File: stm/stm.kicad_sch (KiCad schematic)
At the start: 0 parts

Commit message: added power sch
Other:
- added sheet power (power.kicad_sch)
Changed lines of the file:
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@@
+	)
+	(sheet
+		(at 57.15 93.98)
+		(size 53.34 30.48)
+		(exclude_from_sim no)
+		(in_bom yes)
+		(on_board yes)
+		(dnp no)
+		(fields_autoplaced yes)
+		(stroke
+			(width 0.1524)
+			(type solid)
+		)
+		(fill
+			(color 0 0 0 0.0000)
+		)
+		(property "Sheetname" "power"
+			(at 57.15 93.2684 0)
+			(effects
+				(font
+					(size 1.27 1.27)
+				)
+				(justify left bottom)
+			)
+		)
+		(property "Sheetfile" "power.kicad_sch"
+			(at 57.15 125.0446 0)
+			(effects
+				(font
+					(size 1.27 1.27)
+				)
+				(justify left top)
+			)
+		)
+		(instances
+			(project "stm"
+				(path "/8c38e4ab-00b4-41d2-ba83-c24ee9e4f60d"
+					(page "4")
+				)
+			)
+		)
 	)
 	(sheet

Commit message: usbc power and uart
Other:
- added sheet peripherals (peripherals.kicad_sch)
- added sheet usb to uart (usb_to_uart.kicad_sch)
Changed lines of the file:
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@@
 	(paper "A")
+	(sheet
+		(at 123.19 93.98)
+		(size 52.07 30.48)
+		(exclude_from_sim no)
+		(in_bom yes)
+		(on_board yes)
+		(dnp no)
+		(fields_autoplaced yes)
+		(stroke
+			(width 0.1524)
+			(type solid)
+		)
+		(fill
+			(color 0 0 0 0.0000)
+		)
+		(property "Sheetname" "peripherals"
+			(at 123.19 93.2684 0)
+			(effects
+				(font
+					(size 1.27 1.27)
+				)
+				(justify left bottom)
+			)
+		)
+		(property "Sheetfile" "peripherals.kicad_sch"
+			(at 123.19 125.0446 0)
+			(effects
+				(font
+					(size 1.27 1.27)
+				)
+				(justify left top)
+			)
+		)
+		(instances
+			(project "stm"
+				(path "/8c38e4ab-00b4-41d2-ba83-c24ee9e4f60d"
+					(page "5")
+				)
+			)
+		)
+	)
 	(sheet
 		(at 57.15 49.53)
@@
 				)
 			)
+		)
+	)
+	(sheet
+		(at 181.61 93.98)
+		(size 44.45 30.48)
+		(exclude_from_sim no)
+		(in_bom yes)
+		(on_board yes)
+		(dnp no)
+		(fields_autoplaced yes)
+		(stroke
+			(width 0.1524)
+			(type solid)
+		)
+		(fill
+			(color 0 0 0 0.0000)
+		)
+		(property "Sheetname" "usb to uart"
+			(at 181.61 93.2684 0)
+			(effects
+				(font
+					(size 1.27 1.27)
+				)
+				(justify left bottom)
+			)
+		)
+		(property "Sheetfile" "usb_to_uart.kicad_sch"
+			(at 181.61 125.0446 0)
+			(effects
+				(font
+					(size 1.27 1.27)
+				)
+				(justify left top)
+			)
+		)
+		(instances
+			(project "stm"
+				(path "/8c38e4ab-00b4-41d2-ba83-c24ee9e4f60d"
+					(page "6")
+				)
+			)

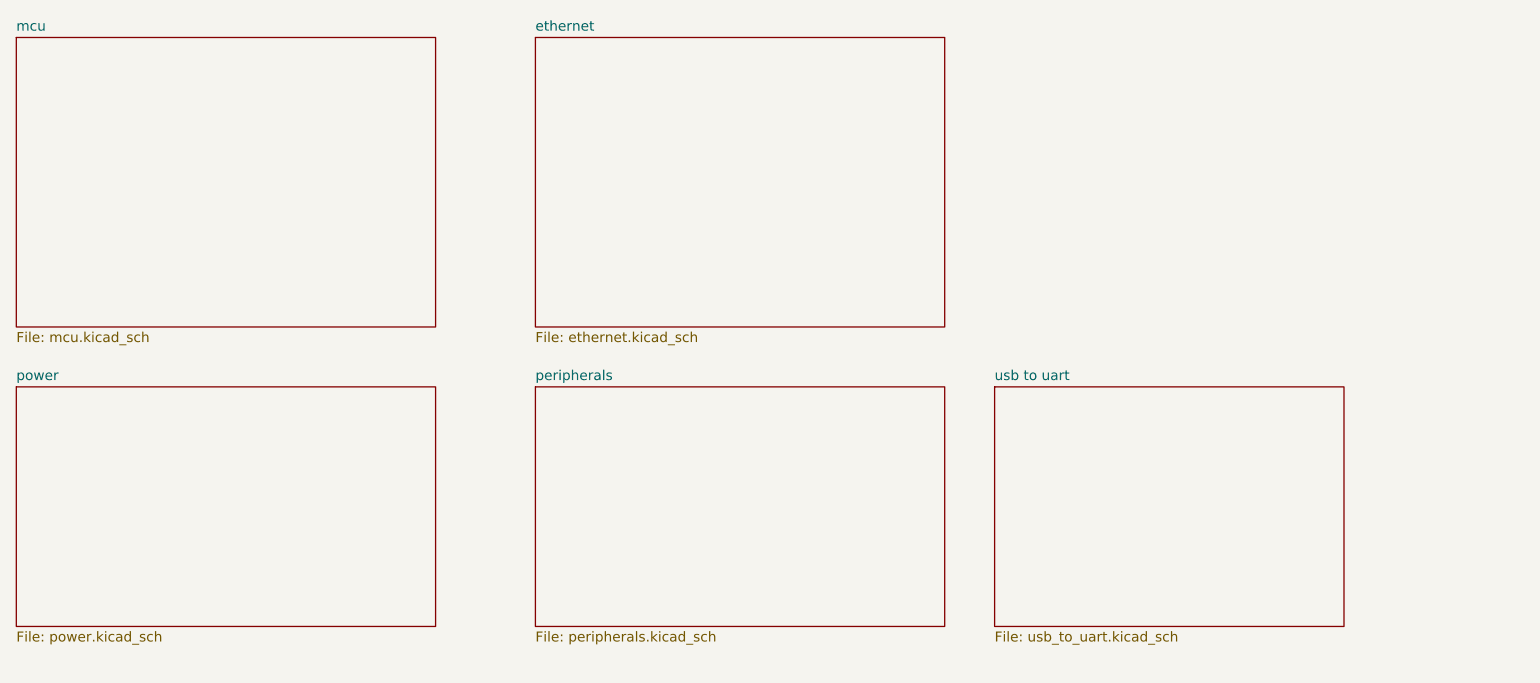
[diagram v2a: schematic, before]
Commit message: PE and PF pin connectors
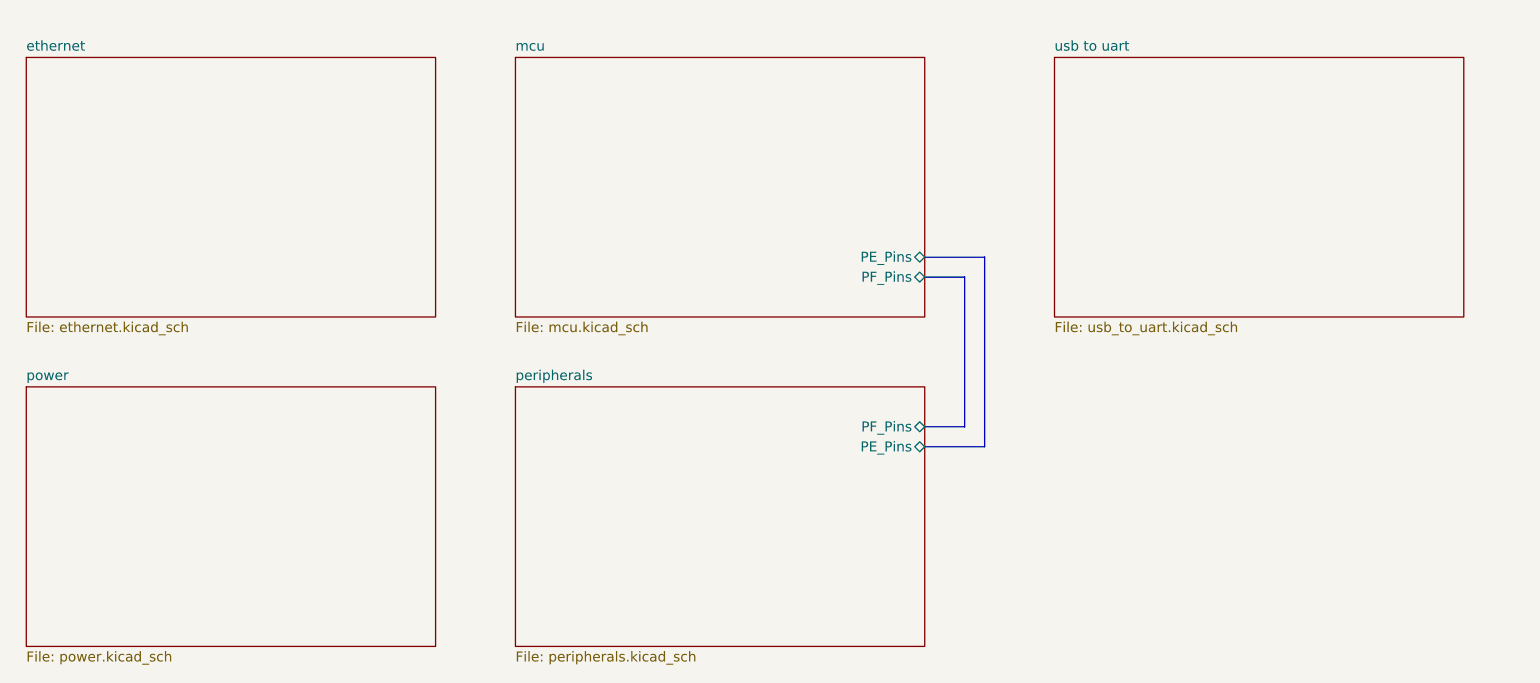
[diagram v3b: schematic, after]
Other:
- sheet mcu ports: added PE_Pins, PF_Pins; removed none
- sheet peripherals ports: added PE_Pins, PF_Pins; removed none
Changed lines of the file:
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@@
 	(generator_version "9.0")
 	(paper "A")
-	(sheet
-		(at 123.19 93.98)
-		(size 52.07 30.48)
+	(bus
+		(pts
+			(xy 177.8 99.06) (xy 177.8 80.01)
+		)
+		(stroke
+			(width 0)
+			(type default)
+		)
+	)
+	(bus
+		(pts
+			(xy 177.8 99.06) (xy 172.72 99.06)
+		)
+		(stroke
+			(width 0)
+			(type default)
+		)
+	)
+	(bus
+		(pts
+			(xy 172.72 77.47) (xy 180.34 77.47)
+		)
+		(stroke
+			(width 0)
+			(type default)
+		)
+	)
+	(bus
+		(pts
+			(xy 172.72 80.01) (xy 177.8 80.01)
+		)
+		(stroke
+			(width 0)
+			(type default)
+		)
+	)
+	(bus
+		(pts
+			(xy 180.34 77.47) (xy 180.34 101.6)
+		)
+		(stroke
+			(width 0)
+			(type default)
+		)
+	)
+	(bus
+		(pts
+			(xy 180.34 101.6) (xy 172.72 101.6)
+		)
+		(stroke
+			(width 0)
+			(type default)
+		)
+	)
+	(sheet
+		(at 120.65 93.98)
+		(size 52.07 33.02)
 		(exclude_from_sim no)
 		(in_bom yes)
@@
 		)
 		(property "Sheetname" "peripherals"
-			(at 123.19 93.2684 0)
+			(at 120.65 93.2684 0)
 			(effects
 				(font
@@
 		)
 		(property "Sheetfile" "peripherals.kicad_sch"
-			(at 123.19 125.0446 0)
-			(effects
-				(font
-					(size 1.27 1.27)
-				)
-				(justify left top)
+			(at 120.65 127.5846 0)
+			(effects
+				(font
+					(size 1.27 1.27)
+				)
+				(justify left top)
+			)
+		)
+		(pin "PE_Pins" bidirectional
+			(at 172.72 101.6 0)
+			(effects
+				(font
+					(size 1.27 1.27)
+				)
+				(justify right)
+			)
+		)
+		(pin "PF_Pins" bidirectional
+			(at 172.72 99.06 0)
+			(effects
+				(font
+					(size 1.27 1.27)
+				)
+				(justify right)
 			)
 		)
@@
 	)
 	(sheet
-		(at 57.15 49.53)
-		(size 53.34 36.83)
+		(at 120.65 52.07)
+		(size 52.07 33.02)
 		(exclude_from_sim no)
 		(in_bom yes)
@@
 		)
 		(property "Sheetname" "mcu"
-			(at 57.15 48.8184 0)
+			(at 120.65 51.3584 0)
 			(effects
 				(font
@@
 		)
 		(property "Sheetfile" "mcu.kicad_sch"
-			(at 57.15 86.9446 0)
-			(effects
-				(font
-					(size 1.27 1.27)
-				)
-				(justify left top)
+			(at 120.65 85.6746 0)
+			(effects
+				(font
+					(size 1.27 1.27)
+				)
+				(justify left top)
+			)
+		)
+		(pin "PE_Pins" bidirectional
+			(at 172.72 77.47 0)
+			(effects
+				(font
+					(size 1.27 1.27)
+				)
+				(justify right)
+			)
+		)
+		(pin "PF_Pins" bidirectional
+			(at 172.72 80.01 0)
+			(effects
+				(font
+					(size 1.27 1.27)
+				)
+				(justify right)
 			)
 		)
@@
 	)
 	(sheet
-		(at 57.15 93.98)
-		(size 53.34 30.48)
+		(at 58.42 93.98)
+		(size 52.07 33.02)
 		(exclude_from_sim no)
 		(in_bom yes)
@@
 		)
 		(property "Sheetname" "power"
-			(at 57.15 93.2684 0)
+			(at 58.42 93.2684 0)
 			(effects
 				(font
@@
 		)
 		(property "Sheetfile" "power.kicad_sch"
-			(at 57.15 125.0446 0)
+			(at 58.42 127.5846 0)
 			(effects
 				(font
@@
 	)
 	(sheet
-		(at 123.19 49.53)
-		(size 52.07 36.83)
+		(at 58.42 52.07)
+		(size 52.07 33.02)
 		(exclude_from_sim no)
 		(in_bom yes)
@@
 		)
 		(property "Sheetname" "ethernet"
-			(at 123.19 48.8184 0)
+			(at 58.42 51.3584 0)
 			(effects
 				(font
@@
 		)
 		(property "Sheetfile" "ethernet.kicad_sch"
-			(at 123.19 86.9446 0)
+			(at 58.42 85.6746 0)
 			(effects
 				(font
@@
 	)
 	(sheet
-		(at 181.61 93.98)
-		(size 44.45 30.48)
+		(at 189.23 52.07)
+		(size 52.07 33.02)
 		(exclude_from_sim no)
 		(in_bom yes)
@@
 		)
 		(property "Sheetname" "usb to uart"
-			(at 181.61 93.2684 0)
+			(at 189.23 51.3584 0)
 			(effects
 				(font
@@
 		)
 		(property "Sheetfile" "usb_to_uart.kicad_sch"
-			(at 181.61 125.0446 0)
-			(effects
-				(font
+			(at 189.23 85.6746 0)
+			(effects
+				(font

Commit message: completed peripherals mapping
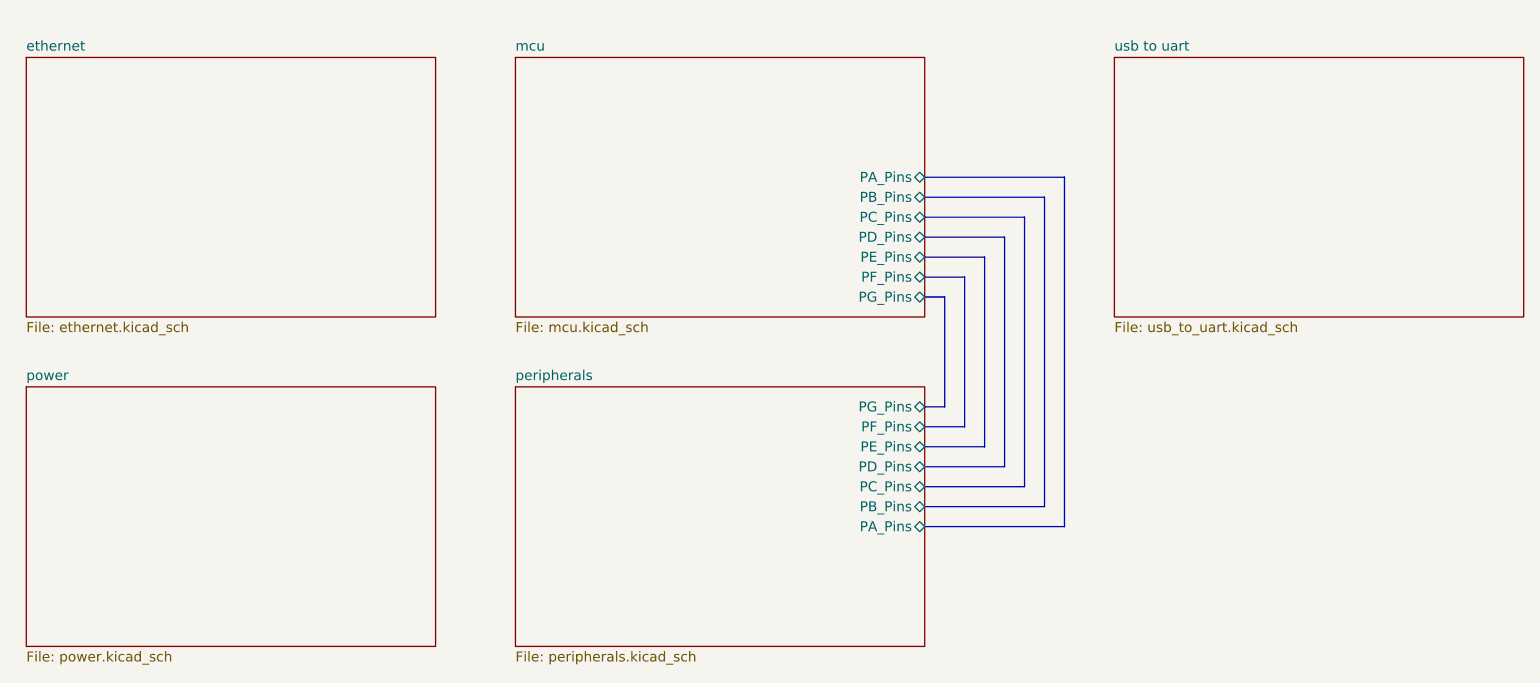
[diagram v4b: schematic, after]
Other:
- sheet mcu ports: added PA_Pins, PB_Pins, PC_Pins, PD_Pins, PG_Pins; removed none
- sheet peripherals ports: added PA_Pins, PB_Pins, PC_Pins, PD_Pins, PG_Pins; removed none
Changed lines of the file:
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@@
+	(bus
+		(pts
+			(xy 187.96 109.22) (xy 187.96 69.85)
+		)
+		(stroke
+			(width 0)
+			(type default)
+		)
+	)
+	(bus
+		(pts
+			(xy 172.72 111.76) (xy 190.5 111.76)
+		)
+		(stroke
+			(width 0)
+			(type default)
+		)
+	)
+	(bus
+		(pts
+			(xy 172.72 104.14) (xy 182.88 104.14)
+		)
+		(stroke
+			(width 0)
+			(type default)
+		)
+	)
+	(bus
+		(pts
+			(xy 172.72 69.85) (xy 187.96 69.85)
+		)
+		(stroke
+			(width 0)
+			(type default)
+		)
+	)
+	(bus
+		(pts
+			(xy 175.26 96.52) (xy 172.72 96.52)
+		)
+		(stroke
+			(width 0)
+			(type default)
+		)
+	)
+	(bus
+		(pts
+			(xy 172.72 67.31) (xy 190.5 67.31)
+		)
+		(stroke
+			(width 0)
+			(type default)
+		)
+	)
+	(bus
+		(pts
+			(xy 172.72 82.55) (xy 175.26 82.55)
+		)
+		(stroke
+			(width 0)
+			(type default)
+		)
+	)
+	(bus
+		(pts
+			(xy 182.88 104.14) (xy 182.88 74.93)
+		)
+		(stroke
+			(width 0)
+			(type default)
+		)
+	)
+	(bus
+		(pts
+			(xy 190.5 67.31) (xy 190.5 111.76)
+		)
+		(stroke
+			(width 0)
+			(type default)
+		)
+	)
+	(bus
+		(pts
+			(xy 185.42 72.39) (xy 185.42 106.68)
+		)
+		(stroke
+			(width 0)
+			(type default)
+		)
+	)
+	(bus
+		(pts
+			(xy 172.72 72.39) (xy 185.42 72.39)
+		)
+		(stroke
+			(width 0)
+			(type default)
+		)
+	)
+	(bus
+		(pts
+			(xy 172.72 109.22) (xy 187.96 109.22)
+		)
+		(stroke
+			(width 0)
+			(type default)
+		)
+	)
 	(bus
 		(pts
@@
 	(bus
 		(pts
+			(xy 172.72 106.68) (xy 185.42 106.68)
+		)
+		(stroke
+			(width 0)
+			(type default)
+		)
+	)
+	(bus
+		(pts
 			(xy 172.72 80.01) (xy 177.8 80.01)
 		)
@@
 		(pts
 			(xy 180.34 101.6) (xy 172.72 101.6)
+		)
+		(stroke
+			(width 0)
+			(type default)
+		)
+	)
+	(bus
+		(pts
+			(xy 172.72 74.93) (xy 182.88 74.93)
+		)
+		(stroke
+			(width 0)
+			(type default)
+		)
+	)
+	(bus
+		(pts
+			(xy 175.26 82.55) (xy 175.26 96.52)
 		)
 		(stroke
@@
 			)
 		)
+		(pin "PG_Pins" bidirectional
+			(at 172.72 96.52 0)
+			(effects
+				(font
+					(size 1.27 1.27)
+				)
+				(justify right)
+			)
+		)
+		(pin "PD_Pins" bidirectional
+			(at 172.72 104.14 0)
+			(effects
+				(font
+					(size 1.27 1.27)
+				)
+				(justify right)
+			)
+		)
+		(pin "PC_Pins" bidirectional
+			(at 172.72 106.68 0)
+			(effects
+				(font
+					(size 1.27 1.27)
+				)
+				(justify right)
+			)
+		)
+		(pin "PB_Pins" bidirectional
+			(at 172.72 109.22 0)
+			(effects
+				(font
+					(size 1.27 1.27)
+				)
+				(justify right)
+			)
+		)
+		(pin "PA_Pins" bidirectional
+			(at 172.72 111.76 0)
+			(effects
+				(font
+					(size 1.27 1.27)
+				)
+				(justify right)
+			)
+		)
 		(instances
 			(project "stm"
@@
 			)
 		)
+		(pin "PG_Pins" bidirectional
+			(at 172.72 82.55 0)
+			(effects
+				(font
+					(size 1.27 1.27)
+				)
+				(justify right)
+			)
+		)
+		(pin "PD_Pins" bidirectional
+			(at 172.72 74.93 0)
+			(effects
+				(font
+					(size 1.27 1.27)
+				)
+				(justify right)
+			)
+		)
+		(pin "PC_Pins" bidirectional
+			(at 172.72 72.39 0)
+			(effects
+				(font
+					(size 1.27 1.27)
+				)
+				(justify right)
+			)
+		)
+		(pin "PB_Pins" bidirectional
+			(at 172.72 69.85 0)
+			(effects
+				(font
+					(size 1.27 1.27)
+				)
+				(justify right)
+			)
+		)
+		(pin "PA_Pins" bidirectional
+			(at 172.72 67.31 0)
+			(effects
+				(font
+					(size 1.27 1.27)
+				)
+				(justify right)
+			)
+		)
 		(instances
 			(project "stm"
@@
 	)
 	(sheet
-		(at 189.23 52.07)
+		(at 196.85 52.07)
 		(size 52.07 33.02)
 		(exclude_from_sim no)
@@
 		)
 		(property "Sheetname" "usb to uart"
-			(at 189.23 51.3584 0)
+			(at 196.85 51.3584 0)
 			(effects
 				(font
@@
 		)
 		(property "Sheetfile" "usb_to_uart.kicad_sch"
-			(at 189.23 85.6746 0)
-			(effects
-				(font
+			(at 196.85 85.6746 0)
+			(effects
+				(font
